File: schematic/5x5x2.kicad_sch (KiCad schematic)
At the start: 144 parts, among them SW11 SW, SW12 SW, SW13 SW, SW14 SW, SW15 SW, SW21 SW, SW22 SW, SW23 SW, SW24 SW, SW25 SW, SW31 SW, SW41 SW, SW42 SW, SW43 SW, SW44 SW, SW45 SW, SW51 SW, SW52 SW, SW53 SW, SW54 SW, SW55 SW

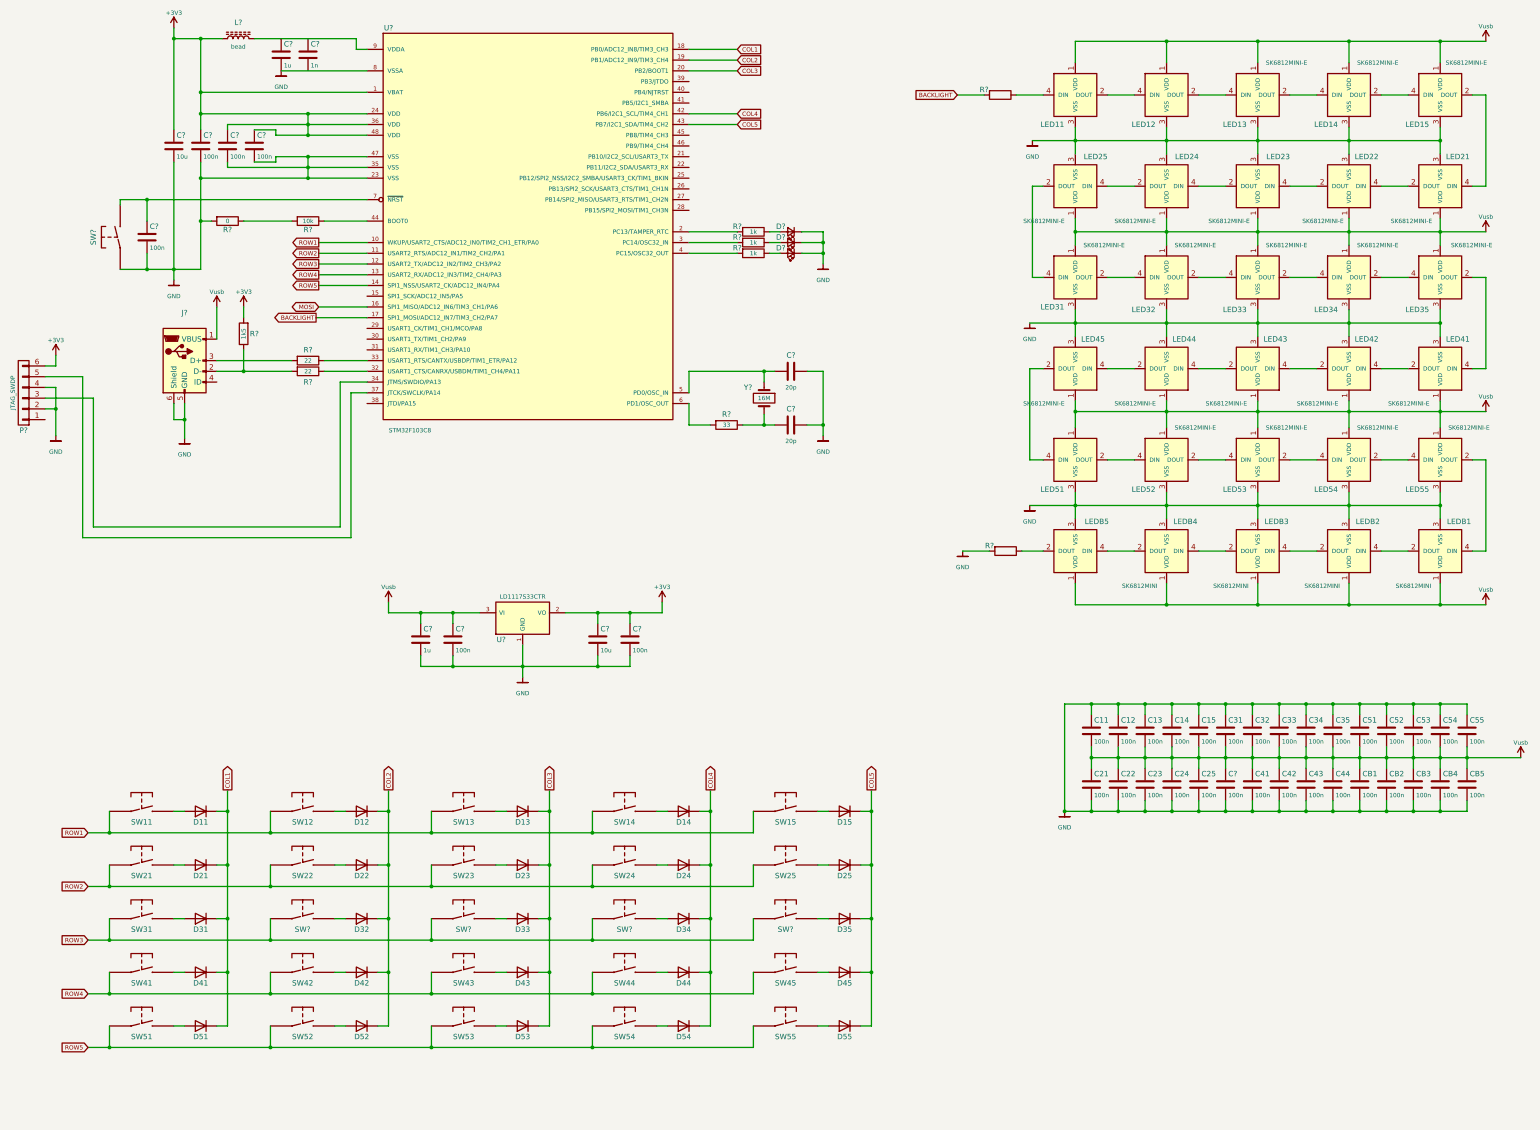
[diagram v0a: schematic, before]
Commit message: Added rotary encoder
Also added optional components when using clones.

Rotary encoder ideas and schematic symbol came from YAEMK -- check
license if allowed, else redraw.
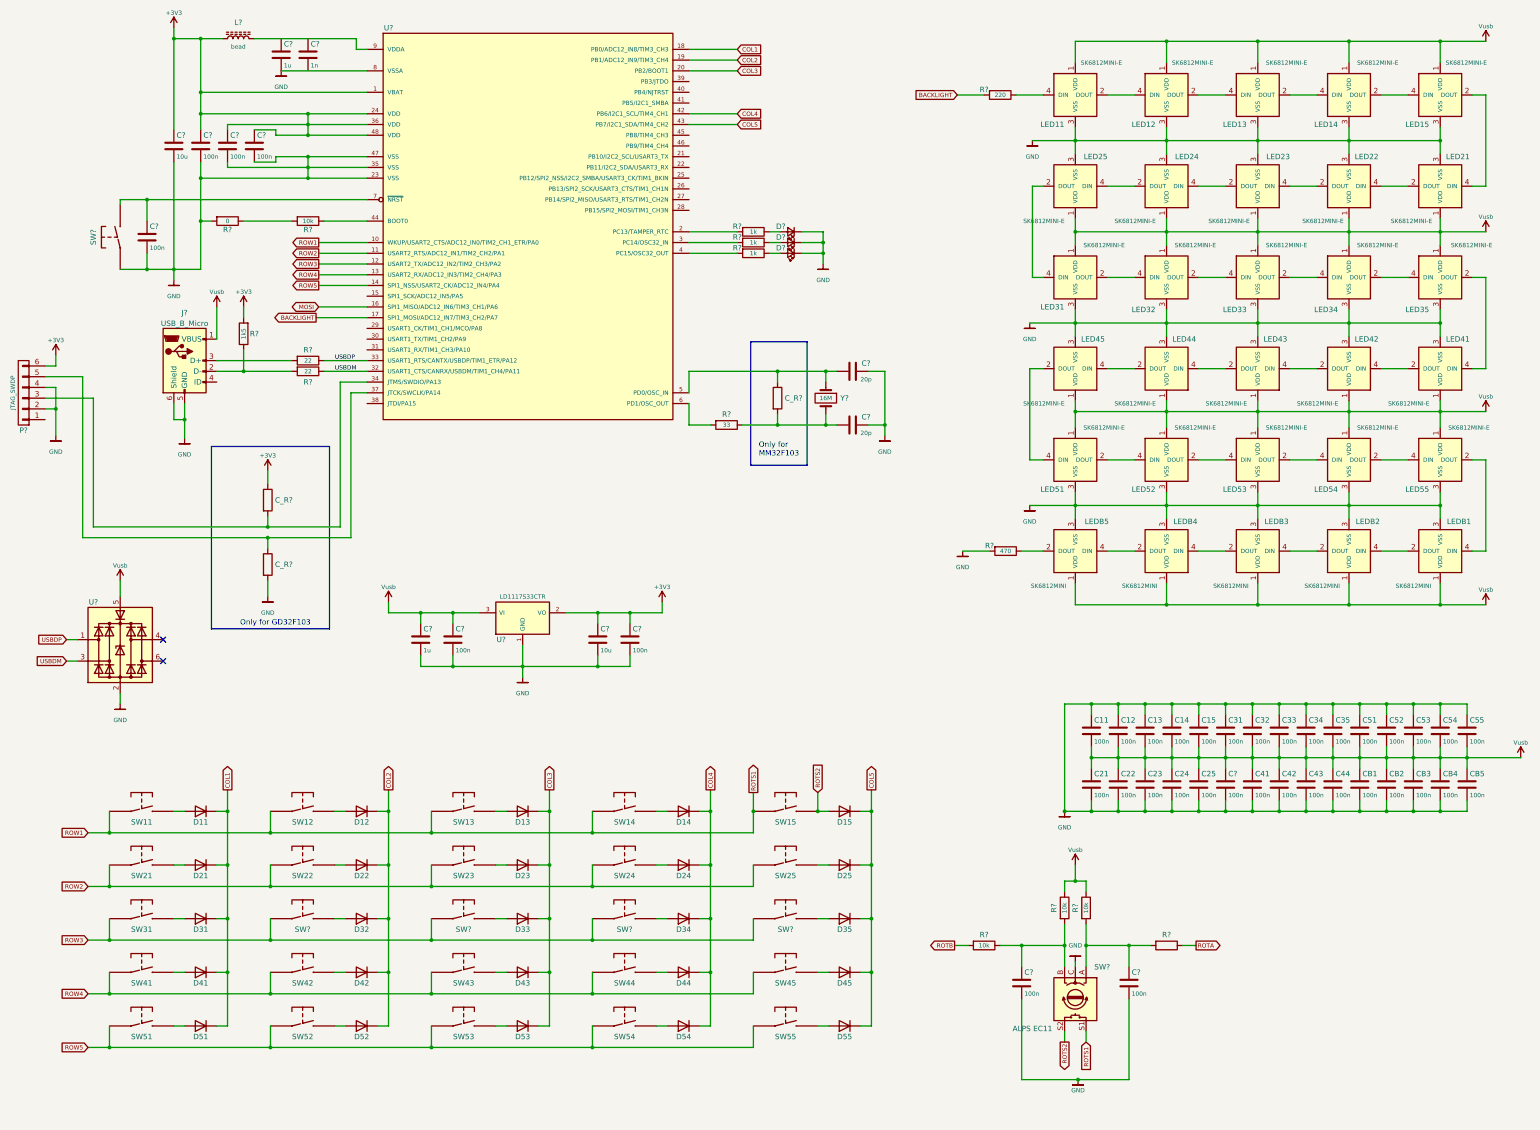
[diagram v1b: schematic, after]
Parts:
- added C? (x2): 100n, Capacitors_SMD:C_1206, symbol Device:C
- added C_R? (x3), R?: (no value), Resistors_SMD:R_0805, symbol Device:R
- added R? (x3): 10k, Resistors_SMD:R_0805, symbol Device:R
- added SW?: ALPS EC11, prettylib:RotaryEncoder_Alps_EC11E-Switch_Vertical_H20mm, symbol YAEMK:Rotary_Encoder_Switch
- added U?: (no value), prettylib:SOT-23-6, symbol YAEMK:SRV0504
- J?: value (none) -> USB_B_Micro
- LED11, LED51: value (none) -> SK6812MINI-E
- LED12: value (none) -> SK6812MINI-E; footprint (none) -> kbd:YS-SK6812MINI-E
- LEDB5: value (none) -> SK6812MINI; footprint (none) -> SK68xx:SK6812MINI
- R?: value (none) -> 470; footprint (none) -> Resistors_SMD:R_0805
- R?: value (none) -> 220
- U?: value STM32F103C8 -> (none)
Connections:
- net +3V3: now also C_R?.1
- net GND: now also C?.2, C?.2, C_R?.2, SW?.C, U?.2 (GND)
- net Vusb: now also R?.1, R?.1, U?.5 (VBUS)
- net USBDP: now reaches R?.1, U?.33 (USART1_RTS/CANTX/USBDP/TIM1_ETR/PA12)
- net USBDP: now also U?.1 (I/O1)
- net at P?.3 (P3), U?.34 (JTMS/SWDIO/PA13): now also C_R?.2
- net at P?.5 (P5), U?.37 (JTCK/SWCLK/PA14): now also C_R?.1
- net at C?.2, R?.1, Y?.2: now also C_R?.2
- net at C?.2, U?.5 (PD0/OSC_IN), Y?.1: now also C_R?.1
- net USBDM: now reaches R?.1, U?.32 (USART1_CTS/CANRX/USBDM/TIM1_CH4/PA11)
- net USBDM: now also U?.3 (I/O2)
- net ROTS2: now reaches D15.2 (A), SW15.2
- net ROTS2: now also SW?.S2
- net ROW1 renamed ROTS1
- net ROTS1: now also SW?.S1
- new net: C?.1, R?.2, R?.2, SW?.A
- new net: C?.1, R?.1, R?.2, SW?.B
- new net ROTA: R?.1
- new net ROTB: R?.2
- no-connect marks 0 -> 2
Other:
- note added: "Only for GD32F103"
- note added: "Only for MM32F103"
- moved on the sheet: C?, Y?

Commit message: Schematic now has usb-c, rotarty encoder and usb tvs protection.
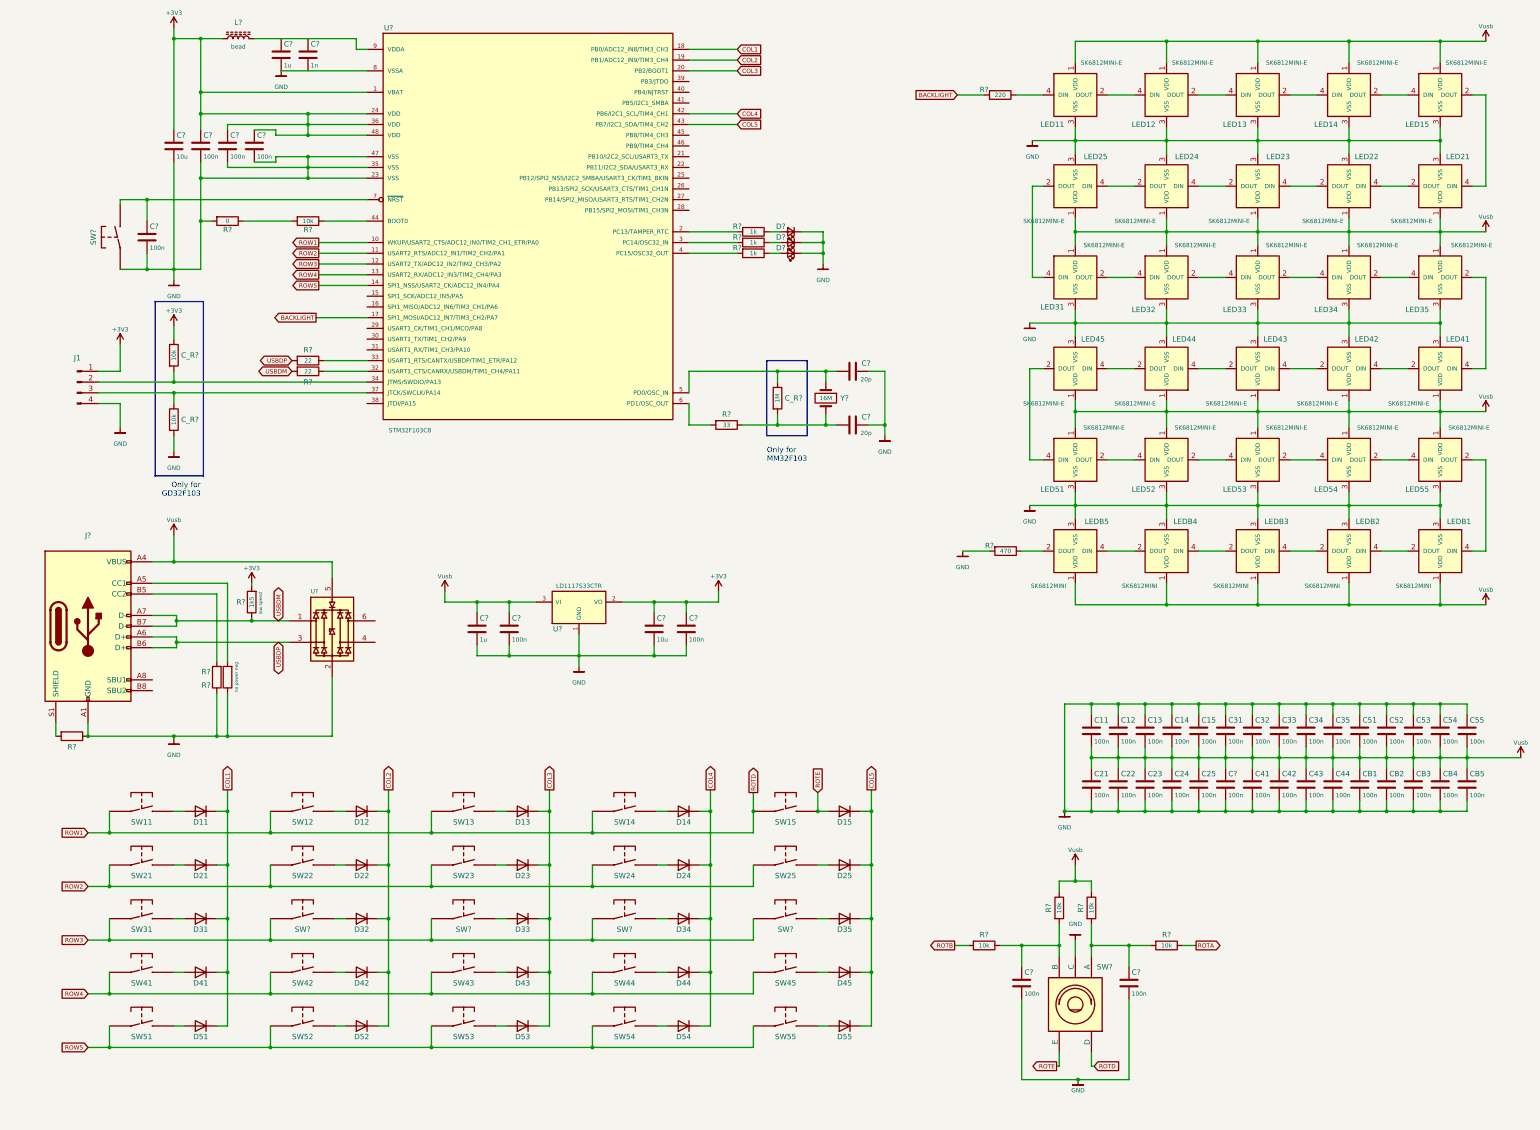
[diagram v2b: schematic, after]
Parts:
- removed J?: USB_B_Micro, symbol Connector:USB_B_Micro
- removed P?: JTAG_SWDP, WD_Packages:TC2030-IDC-NL, symbol jtag_swdp:JTAG_SWDP
- removed SW?: ALPS EC11, prettylib:RotaryEncoder_Alps_EC11E-Switch_Vertical_H20mm, symbol YAEMK:Rotary_Encoder_Switch
- removed U?: (no value), prettylib:SOT-23-6, symbol YAEMK:SRV0504
- added J1: (no value), symbol Connector:Conn_01x04_Male
- added J?: (no value), symbol Connector:USB_C_Receptacle_USB2.0
- added R? (x3): (no value), Resistors_SMD:R_0805, symbol Device:R
- added SW?: (no value), symbol ALPS_EC11:ALPS_EC11
- added U?: (no value), symbol SRV0504:SRV0504
- C_R? (x2), R?: value (none) -> 10k
- C_R?: value (none) -> 1M
- U?: value (none) -> STM32F103C8
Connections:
- net +3V3: now also J1.1 (Pin_1)
- net GND: now also J1.4 (Pin_4), J?.A1 (GND), J?.A12 (GND), J?.B1 (GND), J?.B12 (GND), R?.1, R?.1, R?.1, SW?.C, U?.2 (GND)
- net USBDM: now also R?.1, R?.2, J?.A7 (D-), J?.B7 (D-), U?.1 (IO1); no longer R?.1, U?.32 (USART1_CTS/CANRX/USBDM/TIM1_CH4/PA11)
- net USBDP: now also R?.2, J?.A6 (D+), J?.B6 (D+), U?.3 (IO3); no longer R?.1, U?.33 (USART1_RTS/CANTX/USBDP/TIM1_ETR/PA12)
- net Vusb: now also J?.A4 (VBUS), J?.A9 (VBUS), J?.B4 (VBUS), J?.B9 (VBUS), U?.5 (VDD)
- net at C?.1, R?.2, R?.2: now also SW?.A
- net at C_R?.2, U?.34 (JTMS/SWDIO/PA13): now also J1.2 (Pin_2)
- net at C_R?.1, U?.37 (JTCK/SWCLK/PA14): now also J1.3 (Pin_3)
- net at C?.1, R?.1, R?.2: now also SW?.B
- net MOSI: no longer names the net of U?.16 (SPI1_MISO/ADC12_IN6/TIM3_CH1/PA6)
- net ROTS1 renamed ROTD
- net ROTD: now also SW?.D
- net ROTS2 renamed ROTE
- net ROTE: now also SW?.E
- new net: J?.A5 (CC1), R?.2
- new net: R?.1, U?.33 (USART1_RTS/CANTX/USBDP/TIM1_ETR/PA12)
- new net: J?.S1 (SHIELD), R?.2
- new net: J?.B5 (CC2), R?.2
- new net: R?.1, U?.32 (USART1_CTS/CANRX/USBDM/TIM1_CH4/PA11)
- no-connect marks 2 -> 0
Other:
- note added: "low speed"
- note added: "no power neg"
- company: (none) -> dijkstrw
- title: (none) -> 5x5x2
- moved on the sheet: C?, C_R?, R?, U?

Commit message: Add rotary encoder to pa8/pa9 on schematic
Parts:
- J1: value (none) -> SW Debug
- J?: value (none) -> USB_C_Receptacle_USB2.0
- R? (x2): value (none) -> 5k1
- R?: value (none) -> 0
- SW?: value (none) -> ALPS_EC11
- U?: value (none) -> SRV0504
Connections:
- net ROTA: now also U?.29 (USART1_CK/TIM1_CH1/MCO/PA8)
- net ROTB: now also U?.30 (USART1_TX/TIM1_CH2/PA9)
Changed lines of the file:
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@@
     (stroke (width 0) (type default) (color 0 0 0 0))
   )
+  (wire (pts (xy 89.535 95.25) (xy 101.6 95.25))
+    (stroke (width 0) (type default) (color 0 0 0 0))
+  )
   (wire (pts (xy 355.6 50.8) (xy 355.6 53.975))
     (stroke (width 0) (type default) (color 0 0 0 0))
@@
     (stroke (width 0) (type default) (color 0 0 0 0))
   )
+  (wire (pts (xy 89.535 97.79) (xy 101.6 97.79))
+    (stroke (width 0) (type default) (color 0 0 0 0))
+  )
   (wire (pts (xy 89.535 92.71) (xy 101.6 92.71))
     (stroke (width 0) (type default) (color 0 0 0 0))
@@
     )
   )
+  (global_label "ROTA" (shape input) (at 89.535 95.25 180) (fields_autoplaced)
+    (effects (font (size 1.016 1.016)) (justify right))
+    (property "Intersheet References" "${INTERSHEET_REFS}" (id 0) (at 83.8793 95.1865 0)
+      (effects (font (size 1.016 1.016)) (justify right) hide)
+    )
+  )
   (global_label "BACKLIGHT" (shape output) (at 89.535 92.71 180) (fields_autoplaced)
     (effects (font (size 1.016 1.016)) (justify right))
@@
     )
   )
+  (global_label "ROTB" (shape input) (at 89.535 97.79 180) (fields_autoplaced)
+    (effects (font (size 1.016 1.016)) (justify right))
+    (property "Intersheet References" "${INTERSHEET_REFS}" (id 0) (at 83.7341 97.7265 0)
+      (effects (font (size 1.016 1.016)) (justify right) hide)
+    )
+  )
   (global_label "ROW5" (shape output) (at 90.17 85.09 180) (fields_autoplaced)
     (effects (font (size 1.016 1.016)) (justify right))
@@
       (effects (font (size 1.016 1.016)) (justify left))
     )
-    (property "Value" "" (id 1) (at 84.455 175.26 0)
+    (property "Value" "SRV0504" (id 1) (at 84.455 175.26 0)
       (effects (font (size 1.016 1.016)) (justify left))
     )
@@
     (in_bom yes) (on_board yes)
     (property "Reference" "R?" (id 0) (at 63.5 179.705 0))
-    (property "Value" "" (id 1) (at 68.58 177.8 90)
+    (property "Value" "5k1" (id 1) (at 68.58 177.8 90)
       (effects (font (size 1.016 1.016)))
     )
@@
     (in_bom yes) (on_board yes)
     (property "Reference" "R?" (id 0) (at 31.75 194.31 90))
-    (property "Value" "" (id 1) (at 31.75 191.77 90)
+    (property "Value" "0" (id 1) (at 31.75 191.77 90)
       (effects (font (size 1.016 1.016)))
     )
@@
       (effects (font (size 1.27 1.27)) (justify right))
     )
-    (property "Value" "" (id 1) (at 276.86 260.35 90)
+    (property "Value" "ALPS_EC11" (id 1) (at 276.86 260.35 90)
       (effects (font (size 1.27 1.27)) (justify right))
     )
@@
     (in_bom yes) (on_board yes)
     (property "Reference" "J1" (id 0) (at 33.02 102.235 0))
-    (property "Value" "" (id 1) (at 36.195 115.57 0))
+    (property "Value" "SW Debug" (id 1) (at 36.195 115.57 0))
     (property "Footprint" "" (id 2) (at 33.02 107.95 0)
       (effects (font (size 1.27 1.27)) hide)
@@
     (in_bom yes) (on_board yes) (fields_autoplaced)
     (property "Reference" "J?" (id 0) (at 35.56 144.2552 0))
-    (property "Value" "" (id 1) (at 35.56 146.7921 0))
+    (property "Value" "USB_C_Receptacle_USB2.0" (id 1) (at 35.56 146.7921 0))
     (property "Footprint" "" (id 2) (at 39.37 165.735 0)
       (effects (font (size 1.27 1.27)) hide)
@@
     (in_bom yes) (on_board yes)
     (property "Reference" "R?" (id 0) (at 63.5 176.53 0))
-    (property "Value" "" (id 1) (at 66.04 177.8 90)
+    (property "Value" "5k1" (id 1) (at 66.04 177.8 90)
       (effects (font (size 1.016 1.016)))
     )
